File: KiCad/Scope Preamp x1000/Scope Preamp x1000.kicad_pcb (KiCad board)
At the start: 2 copper layers, 47.5 x 26 mm, 20 parts, among them J1 Conn_01x01_Male, J2 Conn_01x01_Male, J3 Conn_01x01_Male, J4 Conn_Coaxial, SW1 SW_SPDT, SW2 SW_SPDT, U1 INA826

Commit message: Minor update
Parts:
- added PCB1: Board_Module, Library:PCB_Board_50x31, Cmts.User at (141.5, 115.0)
- moved SW1 2.50 mm to (150.0, 101.5)
- moved SW2 2.50 mm to (150.0, 128.5)
- moved J4 1.50 mm to (164.0, 115.0)
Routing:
- net Net-(BT1-Pad1): track 23.6 -> 33.7 mm, vias 2 -> 1
- net VEE: track 7.58 -> 10.1 mm
- net VDD: track 7.56 -> 10.1 mm
- net Net-(BT2-Pad2): track 1.75 -> 4.25 mm
- net Net-(J4-Pad1): track 10.4 -> 11.9 mm
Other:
- board size 47.5 x 26 mm -> 50 x 31 mm
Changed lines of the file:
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@@
   (general
     (thickness 1.6)
-    (drawings 4)
+    (drawings 0)
     (tracks 75)
     (zones 0)
-    (modules 20)
-    (nets 16)
+    (modules 21)
+    (nets 20)
   )
   (page A4)
@@
     (38 B.Mask user)
     (39 F.Mask user)
-    (40 Dwgs.User user)
-    (41 Cmts.User user)
-    (42 Eco1.User user)
-    (43 Eco2.User user)
+    (40 Dwgs.User user hide)
+    (41 Cmts.User user hide)
+    (42 Eco1.User user hide)
+    (43 Eco2.User user hide)
     (44 Edge.Cuts user)
     (45 Margin user)
     (46 B.CrtYd user)
     (47 F.CrtYd user)
-    (48 B.Fab user)
-    (49 F.Fab user)
+    (48 B.Fab user hide)
+    (49 F.Fab user hide)
   )
   (setup
-    (last_trace_width 0.2)
+    (last_trace_width 0.4)
     (user_trace_width 0.2)
     (user_trace_width 0.4)
@@
     (solder_mask_min_width 0.25)
     (aux_axis_origin 0 0)
-    (visible_elements FFFFFF7F)
+    (visible_elements 7FFFFFFF)
     (pcbplotparams
       (layerselection 0x010fc_ffffffff)
@@
   (net 14 "Net-(D1-Pad1)")
   (net 15 "Net-(D2-Pad2)")
+  (net 16 "Net-(PCB1-Pad4)")
+  (net 17 "Net-(PCB1-Pad3)")
+  (net 18 "Net-(PCB1-Pad2)")
+  (net 19 "Net-(PCB1-Pad1)")
   (net_class Default "This is the default net class."
     (clearance 0.2)
@@
     (add_net VEE)
   )
+  (module Library:PCB_Board_50x31 (layer Cmts.User)
+    (at 141.5 115)
+    (fp_text reference PCB1 (at 0 0.5) (layer F.SilkS)
+      (effects (font (size 1 1) (thickness 0.15)))
+    )
+    (fp_text value Board_Module (at 0 -0.5) (layer Edge.Cuts)
+      (effects (font (size 1 1) (thickness 0.15)))
+    )
+    (fp_arc (start 21 11.5) (end 21 15.5) (angle -90) (layer Edge.Cuts) (width 0.15))
+    (fp_arc (start -21 11.5) (end -25 11.5) (angle -90) (layer Edge.Cuts) (width 0.15))
+    (fp_arc (start -21 -11.5) (end -21 -15.5) (angle -90) (layer Edge.Cuts) (width 0.15))
+    (fp_arc (start 21 -11.5) (end 25 -11.5) (angle -90) (layer Edge.Cuts) (width 0.15))
+    (fp_line (start -25 11.5) (end -25 -11.5) (layer Edge.Cuts) (width 0.15))
+    (fp_line (start 21 15.5) (end -21 15.5) (layer Edge.Cuts) (width 0.15))
+    (fp_line (start 25 -11.5) (end 25 11.5) (layer Edge.Cuts) (width 0.15))
+    (fp_line (start -21 -15.5) (end 21 -15.5) (layer Edge.Cuts) (width 0.15))
+    (pad 4 thru_hole circle (at 21 -11.5) (size 6.4 6.4) (drill 3.2) (layers *.Cu *.Mask)
+      (net 16 "Net-(PCB1-Pad4)"))
+    (pad 3 thru_hole circle (at 21 11.5) (size 6.44 6.44) (drill 3.2) (layers *.Cu *.Mask)
+      (net 17 "Net-(PCB1-Pad3)"))
+    (pad 2 thru_hole circle (at -21 11.5) (size 6.4 6.4) (drill 3.2) (layers *.Cu *.Mask)
+      (net 18 "Net-(PCB1-Pad2)"))
+    (pad 1 thru_hole circle (at -21 -11.5) (size 6.4 6.4) (drill 3.2) (layers *.Cu *.Mask)
+      (net 19 "Net-(PCB1-Pad1)"))
+  )
   (module Resistor_SMD:R_0402_1005Metric (layer F.Cu)
     (at 149 118 270)
@@
   )
   (module Button_Switch_SMD:SW_SPDT_CK-JS102011SAQN (layer F.Cu)
-    (at 150 126)
+    (at 150 128.5)
     (descr http://www.ckswitches.com/media/1422/js.pdf)
     (tags "switch spdt")
@@
   )
   (module Button_Switch_SMD:SW_SPDT_CK-JS102011SAQN (layer F.Cu)
-    (at 150 104 180)
+    (at 150 101.5 180)
     (descr http://www.ckswitches.com/media/1422/js.pdf)
     (tags "switch spdt")
@@
   )
   (module Connector_Coaxial:SMA_Amphenol_132289_EdgeMount (layer F.Cu)
-    (at 162.5 115)
+    (at 164 115)
     (descr http://www.amphenolrf.com/132289.html)
     (tags SMA)
@@
     )
   )
-  (gr_line (start 117.5 102) (end 165 102) (layer Edge.Cuts) (width 0.05))
-  (gr_line (start 117.5 128) (end 117.5 102) (layer Edge.Cuts) (width 0.05))
-  (gr_line (start 165 128) (end 117.5 128) (layer Edge.Cuts) (width 0.05))
-  (gr_line (start 165 102) (end 165 128) (layer Edge.Cuts) (width 0.05))
   (segment (start 151.015 111.515) (end 151.03 111.5) (width 0.4) (layer F.Cu) (net 1))
   (segment (start 151.015 115.385) (end 151.015 115.485) (width 0.4) (layer F.Cu) (net 1))
@@
   (segment (start 152.5 109.5) (end 152.5 106.75) (width 0.4) (layer F.Cu) (net 2))
   (segment (start 152 110) (end 152.5 109.5) (width 0.4) (layer F.Cu) (net 2))
+  (segment (start 152.5 106.75) (end 152.5 104.25) (width 0.4) (layer F.Cu) (net 2))
   (segment (start 152.2 115.975) (end 152.2 116.8) (width 0.4) (layer F.Cu) (net 3))
   (segment (start 151.985 117.015) (end 151.985 118.5) (width 0.4) (layer F.Cu) (net 3))
   (segment (start 152.2 116.8) (end 151.985 117.015) (width 0.4) (layer F.Cu) (net 3))
-  (segment (start 151.985 118.5) (end 151.985 119.985) (width 0.4) (layer F.Cu) (net 3))
-  (segment (start 152.5 120.5) (end 152.5 123.25) (width 0.4) (layer F.Cu) (net 3))
-  (segment (start 151.985 119.985) (end 152.5 120.5) (width 0.4) (layer F.Cu) (net 3))
+  (segment (start 151.985 119.985) (end 151.985 118.5) (width 0.4) (layer F.Cu) (net 3))
+  (segment (start 152.5 125.75) (end 152.5 120.5) (width 0.4) (layer F.Cu) (net 3))
+  (segment (start 152.5 120.5) (end 151.985 119.985) (width 0.4) (layer F.Cu) (net 3))
   (segment (start 152.2 114.675) (end 156.675 114.675) (width 0.2) (layer F.Cu) (net 4))
-  (segment (start 157 115) (end 162.5 115) (width 0.2) (layer F.Cu) (net 4))
   (segment (start 156.675 114.675) (end 157 115) (width 0.2) (layer F.Cu) (net 4))
+  (segment (start 157 115) (end 164 115) (width 0.2) (layer F.Cu) (net 4))
   (segment (start 130.015 115) (end 123.5 115) (width 0.4) (layer F.Cu) (net 5))
   (segment (start 145.66 115.325) (end 145.5 115.485) (width 0.2) (layer F.Cu) (net 6))
@@
   (segment (start 142.5 105.45) (end 142.5 105) (width 0.4) (layer B.Cu) (net 8))
   (via (at 142.5 105) (size 0.8) (drill 0.4) (layers F.Cu B.Cu) (net 8))
-  (segment (start 157.6 105.55) (end 157.5 105.45) (width 0.4) (layer B.Cu) (net 8))
+  (segment (start 150 104.875) (end 150 104.25) (width 0.4) (layer F.Cu) (net 8))
+  (segment (start 147.875 107) (end 150 104.875) (width 0.4) (layer F.Cu) (net 8))
+  (segment (start 144.5 107) (end 147.875 107) (width 0.4) (layer F.Cu) (net 8))
+  (segment (start 142.5 105) (end 144.5 107) (width 0.4) (layer F.Cu) (net 8))
+  (segment (start 145 102.5) (end 142.5 105) (width 0.4) (layer B.Cu) (net 8))
+  (segment (start 154.55 102.5) (end 145 102.5) (width 0.4) (layer B.Cu) (net 8))
+  (segment (start 157.6 105.55) (end 154.55 102.5) (width 0.4) (layer B.Cu) (net 8))
   (segment (start 157.6 108.5) (end 157.6 105.55) (width 0.4) (layer B.Cu) (net 8))
-  (segment (start 157.5 105.45) (end 157.5 105) (width 0.4) (layer B.Cu) (net 8))
-  (via (at 157.5 105) (size 0.8) (drill 0.4) (layers F.Cu B.Cu) (net 8))
-  (segment (start 151.125 105) (end 150 106.125) (width 0.4) (layer F.Cu) (net 8))
-  (segment (start 157.5 105) (end 151.125 105) (width 0.4) (layer F.Cu) (net 8))
-  (segment (start 150 106.125) (end 150 106.75) (width 0.4) (layer F.Cu) (net 8))
-  (segment (start 148.875 105) (end 150 106.125) (width 0.4) (layer F.Cu) (net 8))
-  (segment (start 142.5 105) (end 148.875 105) (width 0.4) (layer F.Cu) (net 8))
-  (segment (start 150 123.25) (end 150 121.5) (width 0.4) (layer F.Cu) (net 9))
   (via (at 150 121.5) (size 0.8) (drill 0.4) (layers F.Cu B.Cu) (net 9))
+  (segment (start 150 125.75) (end 150 121.5) (width 0.4) (layer F.Cu) (net 9))
   (segment (start 146.712499 114.025) (end 147.8 114.025) (width 0.2) (layer F.Cu) (net 11))
   (segment (start 133.5 114) (end 134.275 114.775) (width 0.2) (layer F.Cu) (net 11))
@@
     (polygon
       (pts
-        (xy 165 101.993057) (xy 165 127.993057) (xy 117.5 128.006943) (xy 117.5 102.006943)
+        (xy 166.5 99.5) (xy 166.5 130.5) (xy 116.5 130.5) (xy 116.5 99.5)
       )
     )
@@
     (polygon
       (pts
-        (xy 117.5 102) (xy 165 102) (xy 165 128) (xy 117.5 128)
+        (xy 116.5 99.5) (xy 166.5 99.5) (xy 166.5 130.5) (xy 116.5 130.5)
       )
     )

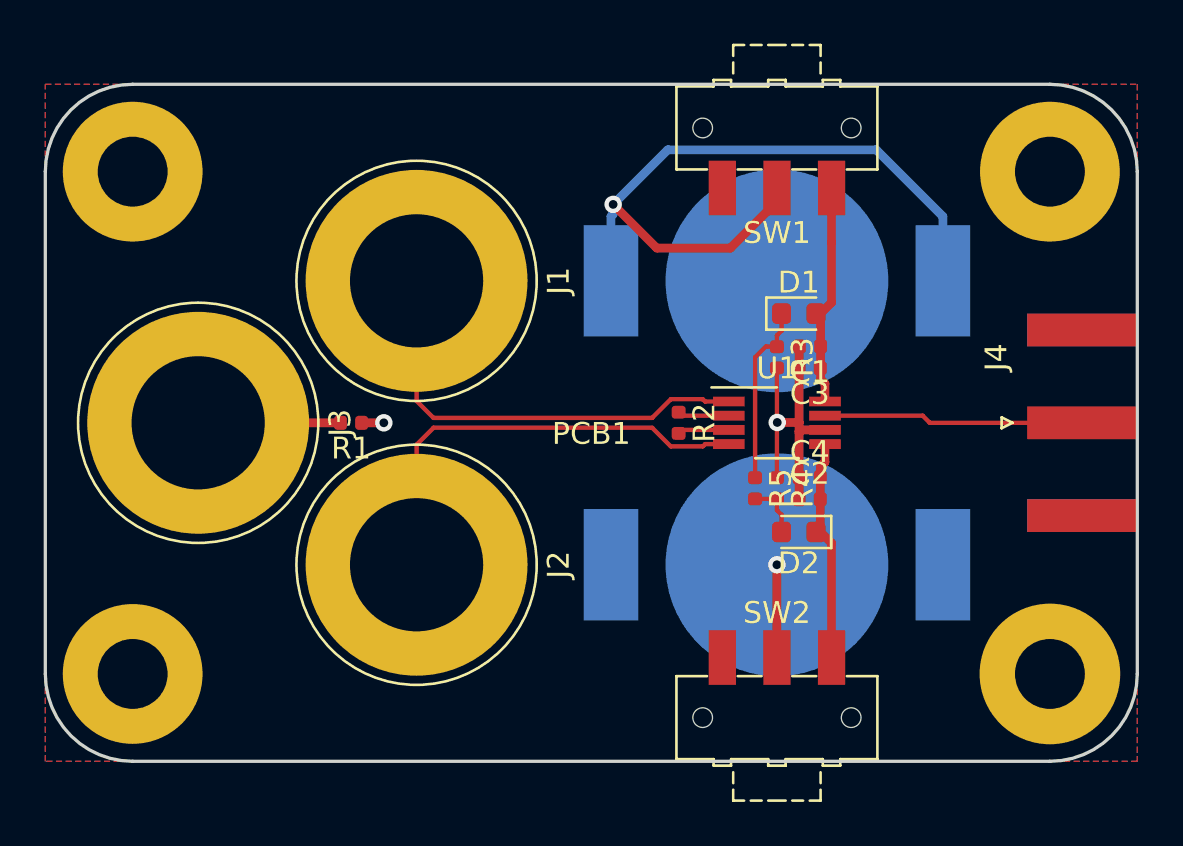
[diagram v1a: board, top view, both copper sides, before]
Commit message: Update gain resistor to achieve x1000
Minor PCB update
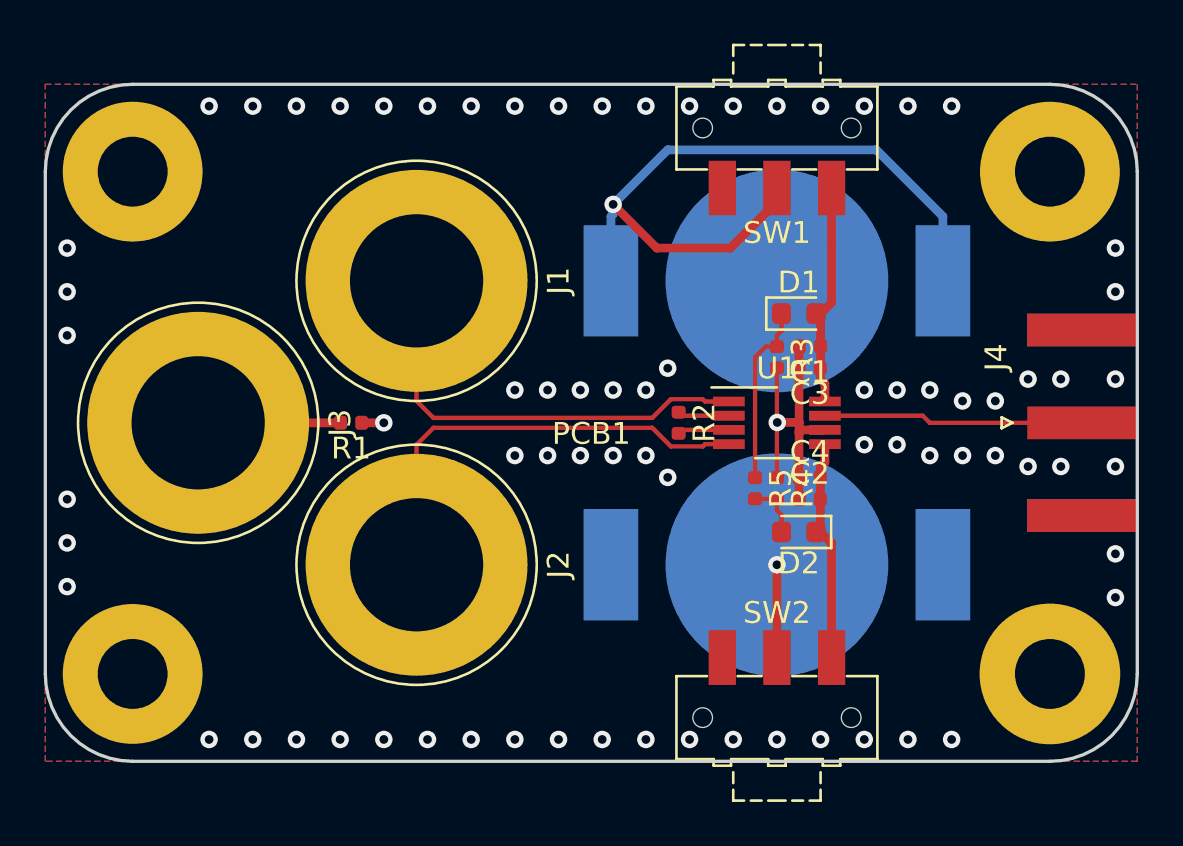
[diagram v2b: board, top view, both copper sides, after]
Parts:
- PCB1: moved to F.Cu
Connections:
- PCB1 pad 1: Net-(PCB1-Pad1) -> GND
- PCB1 pad 2: Net-(PCB1-Pad2) -> GND
- PCB1 pad 3: Net-(PCB1-Pad3) -> GND
- PCB1 pad 4: Net-(PCB1-Pad4) -> GND
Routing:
- net GND: vias 2 -> 76
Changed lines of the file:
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@@
     (thickness 1.6)
     (drawings 0)
-    (tracks 75)
+    (tracks 150)
     (zones 0)
     (modules 21)
-    (nets 20)
+    (nets 16)
   )
   (page A4)
@@
   )
   (setup
-    (last_trace_width 0.4)
+    (last_trace_width 0.25)
     (user_trace_width 0.2)
     (user_trace_width 0.4)
@@
   (net 14 "Net-(D1-Pad1)")
   (net 15 "Net-(D2-Pad2)")
-  (net 16 "Net-(PCB1-Pad4)")
-  (net 17 "Net-(PCB1-Pad3)")
-  (net 18 "Net-(PCB1-Pad2)")
-  (net 19 "Net-(PCB1-Pad1)")
   (net_class Default "This is the default net class."
     (clearance 0.2)
@@
     (add_net VEE)
   )
-  (module Library:PCB_Board_50x31 (layer Cmts.User)
+  (module Library:PCB_Board_50x31 (layer F.Cu)
     (at 141.5 115)
     (fp_text reference PCB1 (at 0 0.5) (layer F.SilkS)
       (effects (font (size 1 1) (thickness 0.15)))
     )
-    (fp_text value Board_Module (at 0 -0.5) (layer Edge.Cuts)
+    (fp_text value Board_Module (at 0 -0.5) (layer F.Fab)
       (effects (font (size 1 1) (thickness 0.15)))
     )
@@
     (fp_line (start -21 -15.5) (end 21 -15.5) (layer Edge.Cuts) (width 0.15))
     (pad 4 thru_hole circle (at 21 -11.5) (size 6.4 6.4) (drill 3.2) (layers *.Cu *.Mask)
-      (net 16 "Net-(PCB1-Pad4)"))
+      (net 1 GND))
     (pad 3 thru_hole circle (at 21 11.5) (size 6.44 6.44) (drill 3.2) (layers *.Cu *.Mask)
-      (net 17 "Net-(PCB1-Pad3)"))
+      (net 1 GND))
     (pad 2 thru_hole circle (at -21 11.5) (size 6.4 6.4) (drill 3.2) (layers *.Cu *.Mask)
-      (net 18 "Net-(PCB1-Pad2)"))
+      (net 1 GND))
     (pad 1 thru_hole circle (at -21 -11.5) (size 6.4 6.4) (drill 3.2) (layers *.Cu *.Mask)
-      (net 19 "Net-(PCB1-Pad1)"))
+      (net 1 GND))
   )
   (module Resistor_SMD:R_0402_1005Metric (layer F.Cu)
@@
   (segment (start 151.015 114.985) (end 151.015 111.515) (width 0.4) (layer F.Cu) (net 1))
   (segment (start 151.015 115.485) (end 151.015 114.985) (width 0.4) (layer F.Cu) (net 1))
-  (via (at 150.015 114.985) (size 0.8) (drill 0.4) (layers F.Cu B.Cu) (net 1))
+  (via (at 150.015 114.985) (size 0.8) (drill 0.4) (layers F.Cu B.Cu) (net 1) (status 1000000))
   (segment (start 130.985 115) (end 132 115) (width 0.4) (layer F.Cu) (net 1))
   (via (at 132 115) (size 0.8) (drill 0.4) (layers F.Cu B.Cu) (net 1))
@@
   (segment (start 150 117.515) (end 150 115) (width 0.2) (layer F.Cu) (net 1))
   (segment (start 150 114.97) (end 150.015 114.985) (width 0.2) (layer F.Cu) (net 1))
-  (segment (start 150 112.485) (end 150 114.97) (width 0.2) (layer F.Cu) (net 1))
+  (segment (start 150 112.485) (end 150 114) (width 0.2) (layer F.Cu) (net 1))
+  (via (at 124 129.5) (size 0.8) (drill 0.4) (layers F.Cu B.Cu) (net 1))
+  (via (at 126 129.5) (size 0.8) (drill 0.4) (layers F.Cu B.Cu) (net 1))
+  (via (at 128 129.5) (size 0.8) (drill 0.4) (layers F.Cu B.Cu) (net 1))
+  (via (at 130 129.5) (size 0.8) (drill 0.4) (layers F.Cu B.Cu) (net 1))
+  (via (at 132 129.5) (size 0.8) (drill 0.4) (layers F.Cu B.Cu) (net 1))
+  (via (at 134 129.5) (size 0.8) (drill 0.4) (layers F.Cu B.Cu) (net 1))
+  (via (at 136 129.5) (size 0.8) (drill 0.4) (layers F.Cu B.Cu) (net 1))
+  (via (at 138 129.5) (size 0.8) (drill 0.4) (layers F.Cu B.Cu) (net 1))
+  (via (at 140 129.5) (size 0.8) (drill 0.4) (layers F.Cu B.Cu) (net 1))
+  (via (at 142 129.5) (size 0.8) (drill 0.4) (layers F.Cu B.Cu) (net 1))
+  (via (at 144 129.5) (size 0.8) (drill 0.4) (layers F.Cu B.Cu) (net 1))
+  (via (at 146 129.5) (size 0.8) (drill 0.4) (layers F.Cu B.Cu) (net 1))
+  (via (at 148 129.5) (size 0.8) (drill 0.4) (layers F.Cu B.Cu) (net 1))
+  (via (at 150 129.5) (size 0.8) (drill 0.4) (layers F.Cu B.Cu) (net 1))
+  (via (at 152 129.5) (size 0.8) (drill 0.4) (layers F.Cu B.Cu) (net 1))
+  (via (at 154 129.5) (size 0.8) (drill 0.4) (layers F.Cu B.Cu) (net 1))
+  (via (at 156 129.5) (size 0.8) (drill 0.4) (layers F.Cu B.Cu) (net 1))
+  (via (at 158 129.5) (size 0.8) (drill 0.4) (layers F.Cu B.Cu) (net 1))
+  (via (at 165.5 117) (size 0.8) (drill 0.4) (layers F.Cu B.Cu) (net 1))
+  (via (at 165.5 113) (size 0.8) (drill 0.4) (layers F.Cu B.Cu) (net 1))
+  (via (at 165.5 109) (size 0.8) (drill 0.4) (layers F.Cu B.Cu) (net 1))
+  (via (at 165.5 107) (size 0.8) (drill 0.4) (layers F.Cu B.Cu) (net 1))
+  (via (at 165.5 121) (size 0.8) (drill 0.4) (layers F.Cu B.Cu) (net 1))
+  (via (at 165.5 123) (size 0.8) (drill 0.4) (layers F.Cu B.Cu) (net 1))
+  (via (at 117.5 122.5) (size 0.8) (drill 0.4) (layers F.Cu B.Cu) (net 1))
+  (via (at 117.5 120.5) (size 0.8) (drill 0.4) (layers F.Cu B.Cu) (net 1))
+  (via (at 117.5 118.5) (size 0.8) (drill 0.4) (layers F.Cu B.Cu) (net 1))
+  (via (at 117.5 107) (size 0.8) (drill 0.4) (layers F.Cu B.Cu) (net 1))
+  (via (at 117.5 109) (size 0.8) (drill 0.4) (layers F.Cu B.Cu) (net 1))
+  (via (at 117.5 111) (size 0.8) (drill 0.4) (layers F.Cu B.Cu) (net 1))
+  (via (at 124 100.5) (size 0.8) (drill 0.4) (layers F.Cu B.Cu) (net 1))
+  (via (at 126 100.5) (size 0.8) (drill 0.4) (layers F.Cu B.Cu) (net 1))
+  (via (at 128 100.5) (size 0.8) (drill 0.4) (layers F.Cu B.Cu) (net 1))
+  (via (at 130 100.5) (size 0.8) (drill 0.4) (layers F.Cu B.Cu) (net 1))
+  (via (at 132 100.5) (size 0.8) (drill 0.4) (layers F.Cu B.Cu) (net 1))
+  (via (at 134 100.5) (size 0.8) (drill 0.4) (layers F.Cu B.Cu) (net 1))
+  (via (at 136 100.5) (size 0.8) (drill 0.4) (layers F.Cu B.Cu) (net 1))
+  (via (at 138 100.5) (size 0.8) (drill 0.4) (layers F.Cu B.Cu) (net 1))
+  (via (at 140 100.5) (size 0.8) (drill 0.4) (layers F.Cu B.Cu) (net 1))
+  (via (at 142 100.5) (size 0.8) (drill 0.4) (layers F.Cu B.Cu) (net 1))
+  (via (at 144 100.5) (size 0.8) (drill 0.4) (layers F.Cu B.Cu) (net 1))
+  (via (at 146 100.5) (size 0.8) (drill 0.4) (layers F.Cu B.Cu) (net 1))
+  (via (at 148 100.5) (size 0.8) (drill 0.4) (layers F.Cu B.Cu) (net 1))
+  (via (at 150 100.5) (size 0.8) (drill 0.4) (layers F.Cu B.Cu) (net 1))
+  (via (at 152 100.5) (size 0.8) (drill 0.4) (layers F.Cu B.Cu) (net 1))
+  (via (at 154 100.5) (size 0.8) (drill 0.4) (layers F.Cu B.Cu) (net 1))
+  (via (at 156 100.5) (size 0.8) (drill 0.4) (layers F.Cu B.Cu) (net 1))
+  (via (at 158 100.5) (size 0.8) (drill 0.4) (layers F.Cu B.Cu) (net 1))
+  (via (at 144 113.5) (size 0.8) (drill 0.4) (layers F.Cu B.Cu) (net 1))
+  (via (at 142.5 113.5) (size 0.8) (drill 0.4) (layers F.Cu B.Cu) (net 1))
+  (via (at 141 113.5) (size 0.8) (drill 0.4) (layers F.Cu B.Cu) (net 1))
+  (via (at 139.5 113.5) (size 0.8) (drill 0.4) (layers F.Cu B.Cu) (net 1))
+  (via (at 144 116.5) (size 0.8) (drill 0.4) (layers F.Cu B.Cu) (net 1))
+  (via (at 142.5 116.5) (size 0.8) (drill 0.4) (layers F.Cu B.Cu) (net 1))
+  (via (at 141 116.5) (size 0.8) (drill 0.4) (layers F.Cu B.Cu) (net 1))
+  (via (at 139.5 116.5) (size 0.8) (drill 0.4) (layers F.Cu B.Cu) (net 1))
+  (via (at 145 112.5) (size 0.8) (drill 0.4) (layers F.Cu B.Cu) (net 1))
+  (via (at 145 117.5) (size 0.8) (drill 0.4) (layers F.Cu B.Cu) (net 1))
+  (via (at 154 116) (size 0.8) (drill 0.4) (layers F.Cu B.Cu) (net 1))
+  (via (at 155.5 116) (size 0.8) (drill 0.4) (layers F.Cu B.Cu) (net 1))
+  (via (at 157 116.5) (size 0.8) (drill 0.4) (layers F.Cu B.Cu) (net 1))
+  (via (at 158.5 116.5) (size 0.8) (drill 0.4) (layers F.Cu B.Cu) (net 1))
+  (via (at 160 116.5) (size 0.8) (drill 0.4) (layers F.Cu B.Cu) (net 1))
+  (via (at 161.5 117) (size 0.8) (drill 0.4) (layers F.Cu B.Cu) (net 1))
+  (via (at 163 117) (size 0.8) (drill 0.4) (layers F.Cu B.Cu) (net 1))
+  (via (at 154 113.5) (size 0.8) (drill 0.4) (layers F.Cu B.Cu) (net 1))
+  (via (at 155.5 113.5) (size 0.8) (drill 0.4) (layers F.Cu B.Cu) (net 1))
+  (via (at 157 113.5) (size 0.8) (drill 0.4) (layers F.Cu B.Cu) (net 1))
+  (via (at 158.5 114) (size 0.8) (drill 0.4) (layers F.Cu B.Cu) (net 1))
+  (via (at 160 114) (size 0.8) (drill 0.4) (layers F.Cu B.Cu) (net 1))
+  (via (at 161.5 113) (size 0.8) (drill 0.4) (layers F.Cu B.Cu) (net 1))
+  (via (at 163 113) (size 0.8) (drill 0.4) (layers F.Cu B.Cu) (net 1))
+  (via (at 138 113.5) (size 0.8) (drill 0.4) (layers F.Cu B.Cu) (net 1))
+  (via (at 138 116.5) (size 0.8) (drill 0.4) (layers F.Cu B.Cu) (net 1))
+  (segment (start 150 114) (end 150 114.97) (width 0.2) (layer F.Cu) (net 1))
   (segment (start 152.2 114.025) (end 152.2 113.2) (width 0.4) (layer F.Cu) (net 2))
   (segment (start 152 113) (end 152 111.5) (width 0.4) (layer F.Cu) (net 2))
